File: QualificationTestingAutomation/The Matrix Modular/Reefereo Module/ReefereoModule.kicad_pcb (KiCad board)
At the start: 4 copper layers, 88.9 x 78.7 mm, 119 parts, among them IC1 TUSB2046B, J1 Conn_02x32_Counter_Clockwise_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, J2 OBD Connector, J3 OBD Connector, J6 Conn_02x32_Counter_Clockwise_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, Q1 ULN2003ADR, Q2 2N7002DW, Q3 2N7002DW, Q4 2N7002DW, Q5 2N7002DW, Q6 2N7002DW, Q7 2N7002DW, Q8 2N7002DW, Q9 2N7002DW, SW1 SW_DIP_x04, U1 TC2050-JTAG-SchematicAutomati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, U10 FT2232D-REEL, U11 MAX324CUA, U12 CD4070B, U13 MAX324CUA, U14 CD4070B, U2 AT25SF081-SSHD-X, U3 MSP430G2755IRHA40, U4 SN74HC266DR, U5 SN74LVC08APWR, U6 MAX14752, U7 DG408LE, U8 DS18B20_, U9 DS18B20_, Y1 6MHz, Y2 6MHz

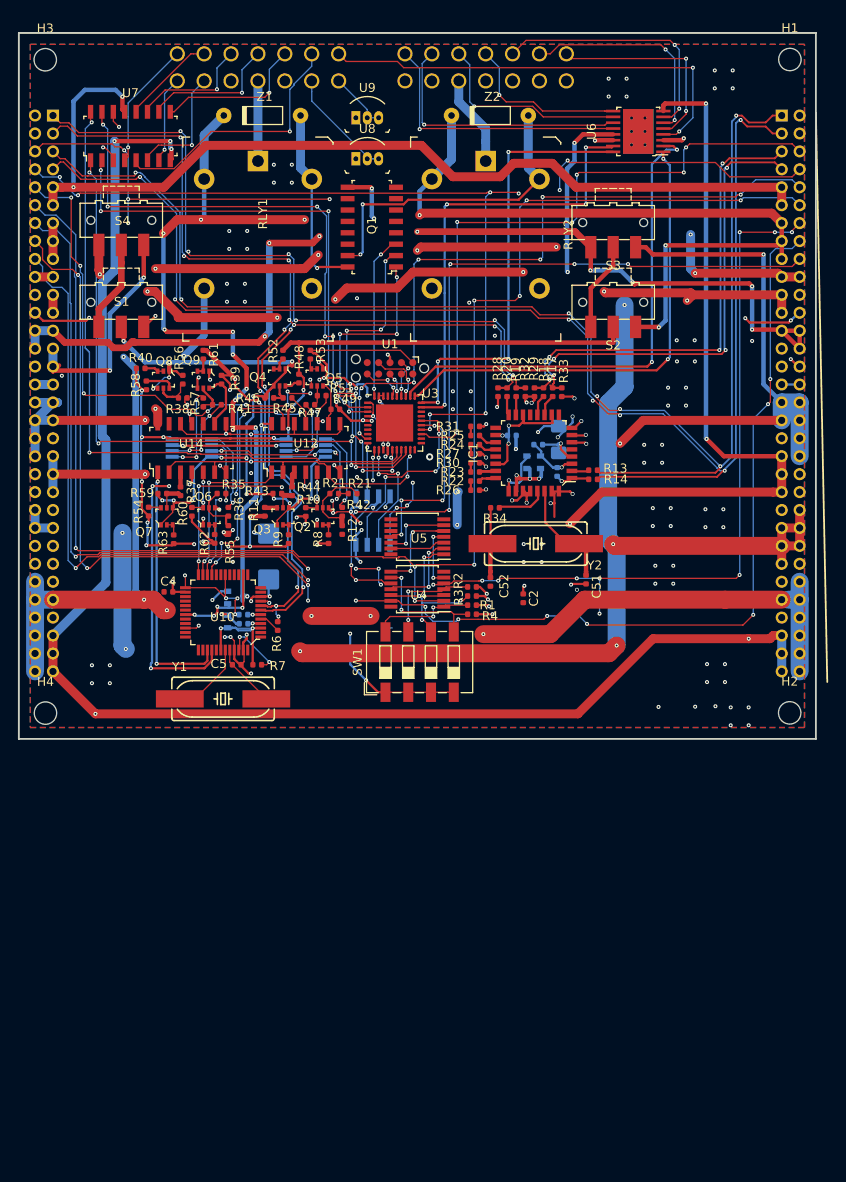
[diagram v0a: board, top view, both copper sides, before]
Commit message: Reefero Module PCB design
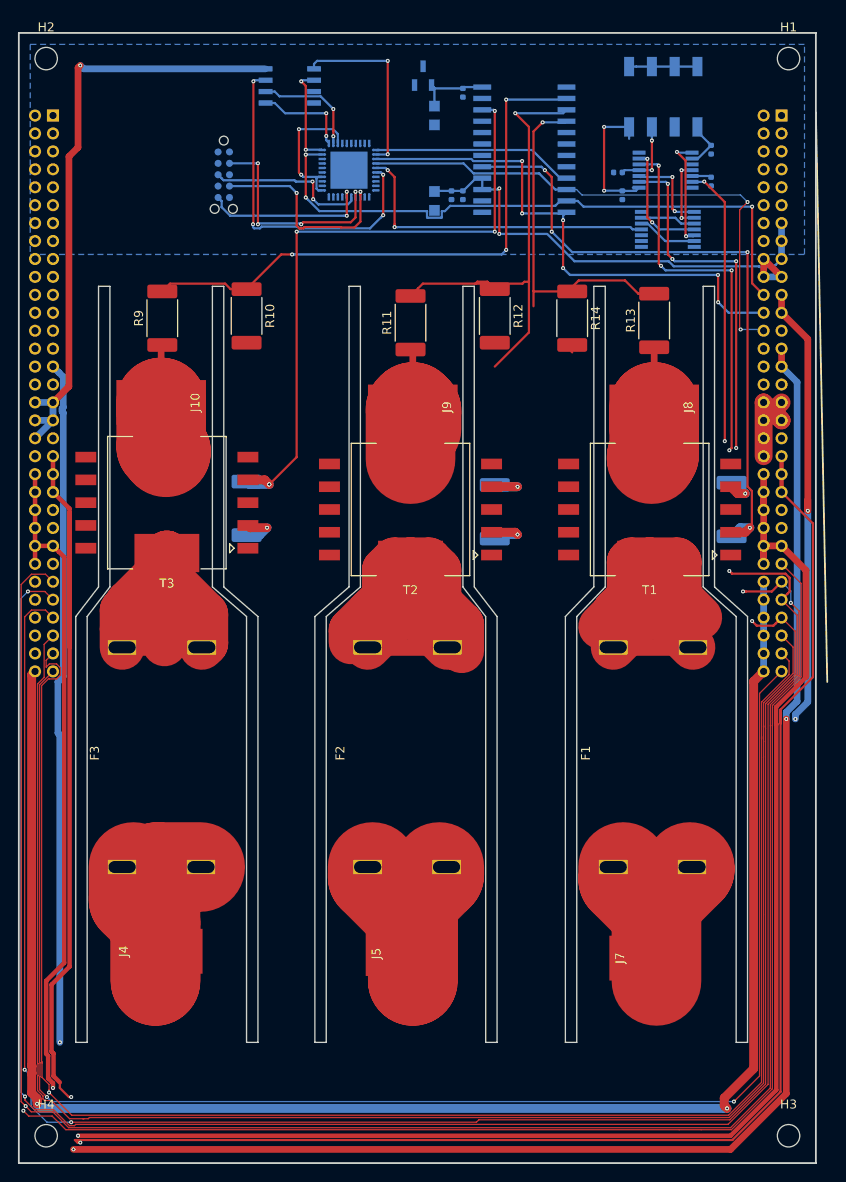
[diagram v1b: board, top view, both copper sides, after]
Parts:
- removed C5: 27pF, Capacitor_SMD:C_0402_1005Metric
- removed C50: 1uF, Capacitor_SMD:C_1206_3216Metric_Pad1.42x1.75mm_HandSolder
- removed C51, C52: 20pF, Capacitor_SMD:C_0402_1005Metric
- removed IC1: TUSB2046B, digikey-footprints:LQFP-32_7x7mm
- removed J2, J3: OBD Connector, .pretty:3MM
- removed L1, L2, L6, L7: L_Core_Ferrite, digikey-footprints:0603
- removed Q1: ULN2003ADR, digikey-footprints:SOIC-16_W3.90mm
- removed Q2, Q3, Q4, Q5, Q6, Q7, Q8, Q9: 2N7002DW, digikey-footprints:SOT-363
- removed R15, R34: 1.5K, Resistor_SMD:R_0402_1005Metric
- removed R16, R26, R27, R28, R29, R30, R31, R32, R33, R50: 15K, Resistor_SMD:R_0402_1005Metric
- removed R17, R18, R19, R20, R22, R23, R24, R25: 22R, Resistor_SMD:R_0402_1005Metric
- removed R21 (x2), R35, R36, R41, R42, R47, R51, R57: R0, Resistor_SMD:R_0402_1005Metric
- removed R37, R38, R39, R40, R44, R45, R48, R49, R52, R53, R54, R58, R60, R61, R62, R63: 100k, Resistor_SMD:R_0402_1005Metric
- removed R43, R46, R56, R59: 56K, Resistor_SMD:R_0402_1005Metric
- removed R55: RESISTOR, Resistor_SMD:R_0402_1005Metric
- removed RLY1, RLY2: G5LE-14_DC5, digikey-footprints:Relay_THT_G5LE-14
- removed S1, S2, S3, S4: ATE1D-2M3-10-Z, Button_Switch_SMD:SW_SPDT_CK-JS102011SAQN
- removed U11, U13: MAX324CUA, Package_SO:MSOP-8_3x3mm_P0.65mm
- removed U12, U14: CD4070B, digikey-footprints:SOIC-14_W3.9mm
- removed U6: MAX14752, digikey-footprints:TSSOP-16-1EP_W4.40mm
- removed U7: DG408LE, digikey-footprints:SOIC-16_W3.90mm
- removed U8, U9: DS18B20_, digikey-footprints:TO-92-3
- removed Y1, Y2: 6MHz, .pretty:HC49UP
- removed Z1, Z2: 1N5231BTR, digikey-footprints:DO-35
- added F1: Fuse, Fuse:0606LittleFuse, F.Cu at (229.1, 99.1)
- added F2: Fuse, Fuse:0606LittleFuse, F.Cu at (201.7, 99.1)
- added F3: Fuse, Fuse:0606LittleFuse, F.Cu at (174.3, 99.1)
- added J10: Conn_01x01_Female, Connector_Wire:SolderWirePad_1x01_SMD_5x10mm, F.Cu at (182.2, 59.9)
- added J4: Conn_01x01_Female, Connector_Wire:SolderWirePad_1x01_SMD_5x10mm, F.Cu at (181.9, 121.2)
- added J5: Conn_01x01_Female, Connector_Wire:SolderWirePad_1x01_SMD_5x10mm, F.Cu at (210.1, 121.4)
- added J7: Conn_01x01_Female, Connector_Wire:SolderWirePad_1x01_SMD_5x10mm, F.Cu at (237.2, 121.9)
- added J8: Conn_01x01_Female, Connector_Wire:SolderWirePad_1x01_SMD_5x10mm, F.Cu at (237.2, 60.5)
- added J9: Conn_01x01_Female, Connector_Wire:SolderWirePad_1x01_SMD_5x10mm, F.Cu at (210.3, 60.5)
- added T1: CST2010_Split, Transformer_SMD:Transformer_Coilcraft_CST2010, F.Cu at (236.7, 71.9)
- added T2: CST2010_Split, Transformer_SMD:Transformer_Coilcraft_CST2010, F.Cu at (210.1, 71.9)
- added T3: CST2010_Split, Transformer_SMD:Transformer_Coilcraft_CST2010, F.Cu at (182.9, 71.1)
- added VR1: LM4040D25FTA, digikey-footprints:SOT-23-3, B.Cu at (211.5, 23.5)
- C1: value 33nF -> 100pF; footprint Capacitor_SMD:C_0402_1005Metric -> .pretty:C_0402_1005Metric
- C2: value 27pF -> 100nF; footprint Capacitor_SMD:C_0402_1005Metric -> .pretty:C_0402_1005Metric; moved to B.Cu
- C3: value 47uF -> 10uF; footprint Capacitor_Tantalum_SMD:CP_EIA-6032-15_Kemet-U_Pad2.25x2.35mm_HandSolder -> .pretty:0805
- C4: value 100nF -> 1uF; footprint Capacitor_SMD:C_0402_1005Metric -> .pretty:0805; moved to B.Cu
- J1: footprint Connector_PinSocket_2.00mm:PinSocket_2x32_P2.00mm_Horizontal -> Connector:PinHeader_2x32_P2.00mm_VerticalOpp
- J6: footprint Connector_PinHeader_2.00mm:PinHeader_2x32_P2.00mm_Horizontal -> Connector:PinHeader_2x32_P2.00mm_VerticalOpp
- R1, R2, R3, R4, SW1, U1, U3, U4, U5: moved to B.Cu
- R10: value 100k -> 5K; footprint Resistor_SMD:R_0402_1005Metric -> Resistor_SMD:R_2512_6332Metric_Pad1.52x3.35mm_HandSolder
- R11, R9: value 100k -> R_US; footprint Resistor_SMD:R_0402_1005Metric -> Resistor_SMD:R_2512_6332Metric_Pad1.52x3.35mm_HandSolder
- R12: value RESISTOR -> 5K; footprint Resistor_SMD:R_0402_1005Metric -> Resistor_SMD:R_2512_6332Metric_Pad1.52x3.35mm_HandSolder
- R13: value 22R -> R_US; footprint Resistor_SMD:R_0402_1005Metric -> Resistor_SMD:R_2512_6332Metric_Pad1.52x3.35mm_HandSolder
- R14: value 22R -> 5K; footprint Resistor_SMD:R_0402_1005Metric -> Resistor_SMD:R_2512_6332Metric_Pad1.52x3.35mm_HandSolder
- R5: value 1K -> YAG5136CT-ND; footprint Resistor_SMD:R_0402_1005Metric -> Resistor_SMD:R_2512_6332Metric_Pad1.52x3.35mm_HandSolder
- R6: value 1.5K -> YAG5136CT-ND; footprint Resistor_SMD:R_0402_1005Metric -> Resistor_SMD:R_2512_6332Metric_Pad1.52x3.35mm_HandSolder; moved to B.Cu
- R7: value 470 -> YAG5136CT-ND; footprint Resistor_SMD:R_0402_1005Metric -> Resistor_SMD:R_2512_6332Metric_Pad1.52x3.35mm_HandSolder; moved to B.Cu
- R8: value 100k -> 1K; footprint Resistor_SMD:R_0402_1005Metric -> .pretty:C_0402_1005Metric; moved to B.Cu
- U10: value FT2232D-REEL -> ADE7758; footprint digikey-footprints:LQFP-48_7x7mm -> Package_SO:SOIC-24W_7.5x15.4mm_P1.27mm; moved to B.Cu
- moved H3 145.9 mm to (252.2, 141.7)
- moved H2 110.5 mm to (169.4, 21.6)
- moved SW1 68.7 mm to (238.3, 25.8), turned to 270 degrees
- moved U10 61.6 mm to (222.8, 31.8), turned to 0 degrees
- moved C4 60.9 mm to (212.7, 27.9), turned to 270 degrees
- moved R4 58.3 mm to (243.6, 31.8), turned to 270 degrees
- moved R5 55.9 mm to (245.9, 71.9), turned to 90 degrees
- moved U4 54.3 mm to (238.5, 34.0), turned to 0 degrees
- moved R3 53.4 mm to (243.6, 35.3), turned to 270 degrees
- moved C1 52.2 mm to (214.6, 36.8), turned to 270 degrees
- moved R8 52.0 mm to (215.9, 25.4)
- moved U2 49.4 mm to (196.6, 24.6), turned to 180 degrees
- moved R2 49.0 mm to (233.2, 34.3), turned to 180 degrees
- moved R1 48.7 mm to (233.7, 36.8), turned to 270 degrees
- moved H4 47.1 mm to (169.4, 141.7)
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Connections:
- C1 pad 1: GND -> +5V
- C1 pad 2: Net-(C1-Pad2) -> GND
- C2 pad 1: GND -> +5V
- C2 pad 2: Net-(C2-Pad2) -> GND
- C3 pad 1: GND -> +5V
- C3 pad 2: +3V3 -> GND
- C4 pad 1: GND -> Net-(C4-Pad1)
- C4 pad 2: +3V3 -> GND
- J1 pad 1: D00- -> +1V8
- J1 pad 10: SCLK0 -> GND
- J1 pad 12: S0 -> GND
- J1 pad 14: S1 -> GND
- J1 pad 16: S2 -> GND
- J1 pad 18: S3 -> -5V
- J1 pad 2: GND -> LO
- J1 pad 22: Net-(J1-Pad22) -> SCLK0
- J1 pad 24: GND -> MISO0
- J1 pad 25: +1V8 -> 1.25V
- J1 pad 26: +1V8 -> MOSI0
- J1 pad 28: +1V8 -> +2V5
- J1 pad 3: D00+ -> +1V8
- J1 pad 4: GND -> LO
- J1 pad 42: Net-(J1-Pad42) -> VD
- J1 pad 44: Net-(J1-Pad44) -> VD
- J1 pad 45: Net-(J1-Pad45) -> GND
- J1 pad 47: VD -> GND
- J1 pad 5: D1+ -> +1V8
- J1 pad 51: VD -> S3
- J1 pad 52: Net-(J1-Pad52) -> VD
- J1 pad 53: Net-(J1-Pad53) -> S2
- J1 pad 55: VDC -> S1
- J1 pad 57: Net-(J1-Pad57) -> S0
- J1 pad 59: LO -> SCLK1
- J1 pad 6: MISO0 -> LO
- J1 pad 61: LO -> MOSI1
- J1 pad 63: LO -> MISO1
- J1 pad 7: D1- -> +12V
- J1 pad 8: MOSI0 -> GND
- J6 pad 1: D2- -> +1V8
- J6 pad 10: SCLK0 -> GND
- J6 pad 12: S0 -> GND
- J6 pad 14: S1 -> GND
- J6 pad 16: S2 -> GND
- J6 pad 18: S3 -> -5V
- J6 pad 2: GND -> LO
- J6 pad 22: Net-(J6-Pad22) -> SCLK0
- J6 pad 24: GND -> MISO0
- J6 pad 25: +1V8 -> 1.25V
- J6 pad 26: +1V8 -> MOSI0
- J6 pad 28: +1V8 -> +2V5
- J6 pad 3: D2+ -> +1V8
- J6 pad 4: GND -> LO
- J6 pad 42: Net-(J6-Pad42) -> VD
- J6 pad 44: Net-(J6-Pad44) -> VD
- J6 pad 45: Net-(J6-Pad45) -> GND
- J6 pad 47: VD -> GND
- J6 pad 5: D00- -> +1V8
- J6 pad 51: VD -> S3
- J6 pad 52: Net-(J6-Pad52) -> VD
- J6 pad 53: Net-(J6-Pad53) -> S2
- J6 pad 55: VDC -> S1
- J6 pad 57: Net-(J6-Pad57) -> S0
- J6 pad 59: LO -> SCLK1
- J6 pad 6: MISO0 -> LO
- J6 pad 61: LO -> MOSI1
- J6 pad 63: LO -> MISO1
- J6 pad 7: D00+ -> +12V
- J6 pad 8: MOSI0 -> GND
- R10 pad 1: Net-(Q2-Pad6) -> /ADE7758/PCS
- R10 pad 2: +3V3 -> GND
- R11 pad 1: 3_RX -> /ADE7758/PBOUT
- R11 pad 2: +VSW -> /ADE7758/PBS
- R12 pad 1: Net-(Q2-Pad5) -> /ADE7758/PBS
- R13 pad 1: D00- -> /ADE7758/PAOUT
- R13 pad 2: /USB/D0- -> /ADE7758/PAS
- R14 pad 1: D00+ -> /ADE7758/PAS
- R14 pad 2: /USB/D0+ -> GND
- R5 pad 1: +5V -> Net-(R5-Pad1)
- R6 pad 2: D2- -> Net-(R6-Pad2)
- R7 pad 1: Net-(L1-Pad2) -> Net-(R7-Pad1)
- R8 pad 2: Net-(Q2-Pad2) -> Net-(C4-Pad1)
- R9 pad 1: +VSW -> /ADE7758/PCOUT
- R9 pad 2: Net-(Q3-Pad2) -> /ADE7758/PCS
- U10 pad 10: +3V3 -> Net-(R7-Pad2)
- U10 pad 11: Net-(U10-Pad11) -> GND
- U10 pad 12: Net-(U10-Pad12) -> Net-(C4-Pad1)
- U10 pad 13: Net-(U10-Pad13) -> GND
- U10 pad 14: Net-(L2-Pad1) -> /ADE7758/PCS
- U10 pad 15: Net-(U10-Pad15) -> /ADE7758/PBS
- U10 pad 16: Net-(U10-Pad16) -> /ADE7758/PAS
- U10 pad 18: GND -> /ADE7758/\IRQ
- U10 pad 2: Net-(U10-Pad2) -> GND
- U10 pad 21: /Serial/sheet5C94BFA4/RTS_3V3 -> CSADE
- U10 pad 22: /Serial/sheet5C94BFA4/CTS_3V3 -> MOSI0
- U10 pad 23: /Serial/sheet5C94BFA4/Tx_3V3 -> SCLK0
- U10 pad 24: /Serial/sheet5C94BFA4/RX_3V3 -> MISO0
- U10 pad 3: Net-(L1-Pad2) -> +5V
- U10 pad 4: Net-(R5-Pad2) -> +5V
- U10 pad 5: Net-(R6-Pad1) -> Net-(R5-Pad1)
- U10 pad 6: Net-(C1-Pad2) -> Net-(R5-Pad2)
- U10 pad 7: D2+ -> Net-(R6-Pad1)
- U10 pad 8: D2- -> Net-(R6-Pad2)
- U10 pad 9: GND -> Net-(R7-Pad1)
- U3 pad 21: Net-(U3-Pad21) -> CSADE
- U3 pad 22: Net-(U3-Pad22) -> /Micro/CSB
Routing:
- net SCLK1: track 0.00 -> 187.7 mm
- net MOSI1: track 0.00 -> 184.7 mm, vias 0 -> 1
- net MISO1: track 0.00 -> 175.5 mm, vias 0 -> 2
- net LO: track 161.7 -> 0.00 mm, vias 5 -> 0
- net D00+: track 159.3 -> 0.00 mm, vias 7 -> 0
- net D00-: track 159.1 -> 0.00 mm, vias 7 -> 0
- net +5V: track 208.2 -> 51.6 mm, vias 17 -> 2
- net -3V3: track 108.8 -> 255.3 mm, vias 2 -> 3
- net GND: track 124.4 -> 0.49 mm, vias 125 -> 0
- net D2-: track 122.7 -> 0.00 mm, vias 11 -> 0
- net VAA: track 147.8 -> 268.0 mm, vias 8 -> 2
- net D2+: track 120.0 -> 0.00 mm, vias 10 -> 0
- net +3V3: track 207.6 -> 89.8 mm, vias 39 -> 1
- net +1V8: track 113.2 -> 0.00 mm, vias 8 -> 0
- net +VSW: track 112.4 -> 0.00 mm, vias 14 -> 0
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- removed copper zone on In2.Cu, net +3V3
- removed copper zone on F.Cu, net GND
- removed copper zone on In1.Cu, net GND
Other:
- board size 88.9 x 78.7 mm -> 88.9 x 126 mm
